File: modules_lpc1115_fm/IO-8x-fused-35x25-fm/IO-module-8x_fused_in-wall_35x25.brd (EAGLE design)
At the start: 35 x 25 mm, 87 parts, among them IC1 LPC1115, IC2 ATAES132A-SHEQ-T, Q2 ASFL, U1 EEPROM, X3 MICROMATCH-10

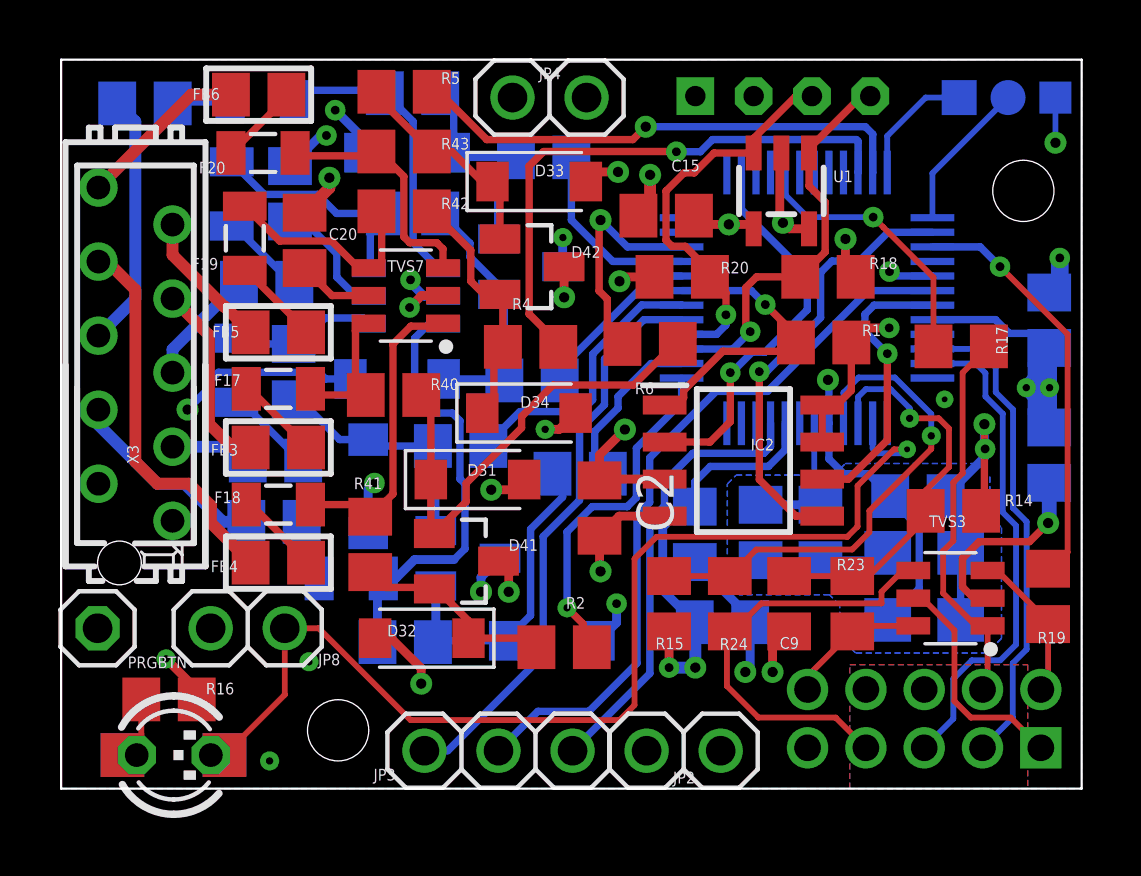
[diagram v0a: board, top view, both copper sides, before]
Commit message: [IOmodule8xUP] - some minor optimizations
corrected mixed up SWDIO / SWCLK labels
optimized some vias
optimized schematic
added ferrite values
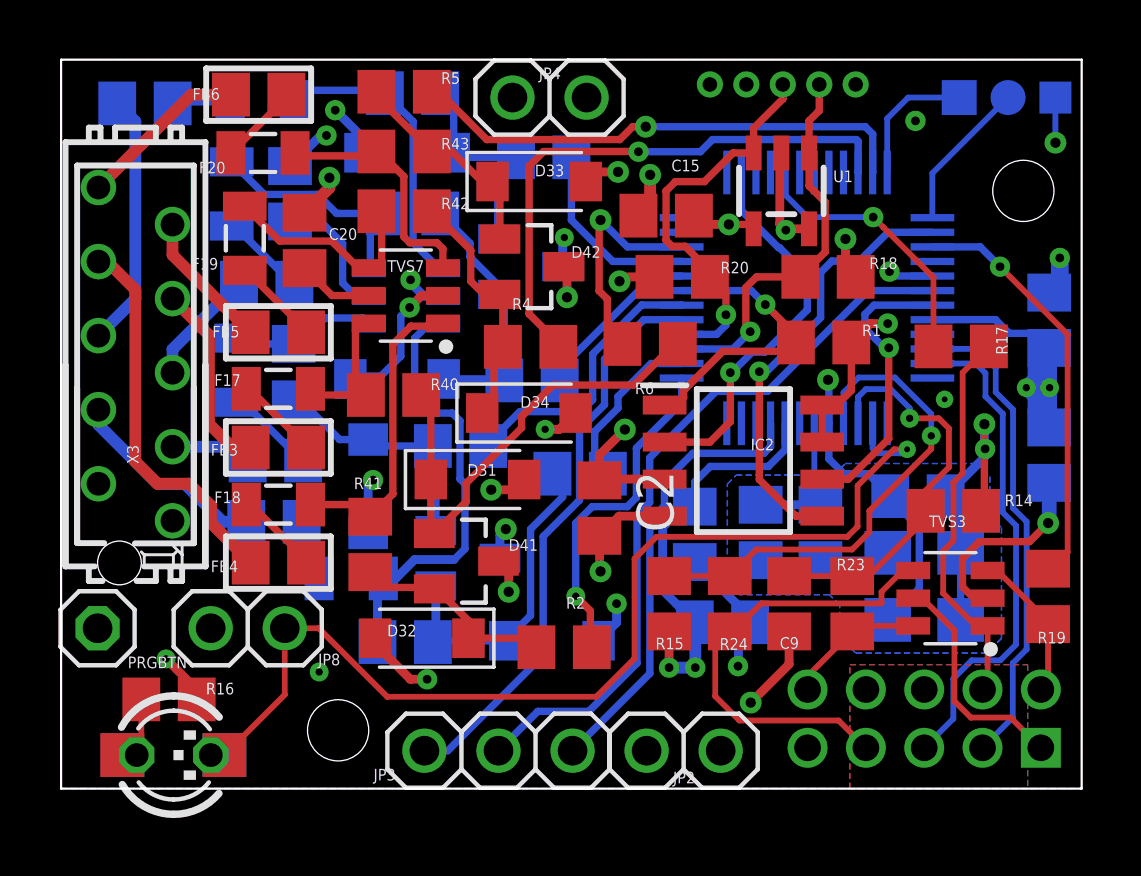
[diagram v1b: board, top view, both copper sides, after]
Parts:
- FB10, FB3, FB4, FB5, FB6, FB7, FB8, FB9: value (none) -> 1.5kΩ@100MHz
- JP1: value B4B-PH-K-S -> 653005114822; device con-JST PH:B4B-PH-K-S -> Wurth_Connectors_WR-WTB:653005114822
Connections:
- net SWD_SWCLK: now also JP7.4, R17.2, TVS3.1; no longer JP7.2, R19.2, TVS3.3
- net SWD_SWDIO: now also JP7.2, R19.2, TVS3.3; no longer JP7.4, R17.2, TVS3.1
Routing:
- net SWD_SWDIO: track 13.4 -> 5.23 mm
- net SWD_SWCLK: track 5.23 -> 13.4 mm
- net PROG: track 38.6 -> 37.0 mm
- net GND: track 60.5 -> 59.5 mm, vias 25 -> 24
- net SWD_ISP_EN: track 14.9 -> 15.7 mm
- net SCL: track 14.0 -> 13.5 mm

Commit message: [IOmodule8xUP] - breaking change of routing, I2C optimization
re-routed some IOs to other ARM pins
added 2nd alternative to connect I2C peripherals
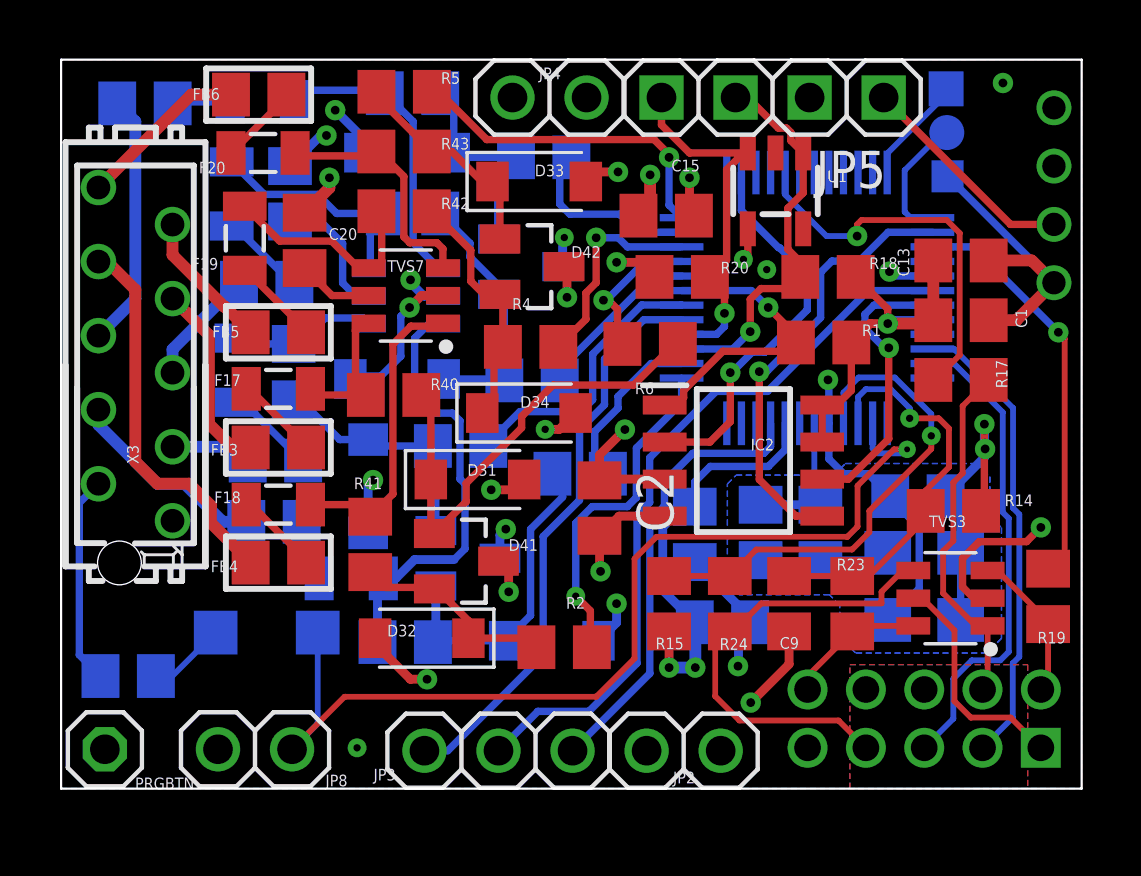
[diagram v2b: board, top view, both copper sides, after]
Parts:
- removed LED2: red, led:LED3MM
- removed LED3: red SMD, led:CHIPLED_1206
- added JP5: (no value), pinhead_dmx:1X04
- JP1: value 653005114822 -> 62000411622; device Wurth_Connectors_WR-WTB:653005114822 -> Eagle_WR-WTB (rev22a):62000411622
- moved JP1 9.34 mm to (33.5, 20.4), turned to 270 degrees
- moved C13 7.33 mm to (30.9, 18.1), flipped to the top, turned to 180 degrees
- moved LED1 5.28 mm to (7.05, 5.35), flipped to the bottom, turned to 90 degrees
- moved GND 4.58 mm to (30.4, 21.0)
- moved JP8 4.16 mm to (6.65, 1.35)
- moved PRGBTN 4.16 mm to (1.50, 1.35)
- moved C1 3.03 mm to (30.9, 16.1), flipped to the top, turned to 180 degrees
- moved RXD 2.42 mm to (30.4, 22.5)
- moved R16 1.61 mm to (2.30, 3.86), flipped to the bottom
- moved R17 1.15 mm to (30.9, 14.0)
- moved TXD 0.54 mm to (30.4, 24.0)
- moved U1 0.20 mm to (24.5, 20.5)
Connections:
- net +3V3: now also JP5.1
- net GND: now also JP5.2
- net IO4: now also IC1.23; no longer IC1.21
- net IO5: now also IC1.21; no longer IC1.22
- net IO7: now also IC1.22; no longer IC1.34
- net IO8: now also IC1.24; no longer IC1.35
- net N$41: no longer LED2.A, LED3.A
- net PROG: no longer LED2.K, LED3.C
- net SCL: now also JP5.3
- net SDA: now also JP5.4
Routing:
- net SDA: track 13.7 -> 27.1 mm
- net SCL: track 13.5 -> 25.9 mm
- net IO7: track 19.4 -> 7.34 mm
- net +3V3: track 65.0 -> 73.0 mm, vias 16 -> 13
- net IO8: track 17.4 -> 11.4 mm
- net SWCLK: track 9.39 -> 13.4 mm
- net IO5: track 7.76 -> 5.17 mm
- net GND: track 59.5 -> 61.8 mm, vias 24 -> 21
- net PROG: track 37.0 -> 34.7 mm
- net SWD_SWCLK: track 13.4 -> 12.2 mm
- net DBG_TXD: track 4.62 -> 3.71 mm
- net DBG_RXD: track 5.19 -> 4.44 mm
- net N$41: track 3.37 -> 2.67 mm
- net ISP_RXD: track 16.5 -> 15.9 mm
- net ISP_TXD: track 17.1 -> 16.5 mm
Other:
- board text added: "IO module fused 8x v1.0.0 beta2"
- board text added: "selfbus.org"

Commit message: [IOmodule8xUP] - changed values to standard values
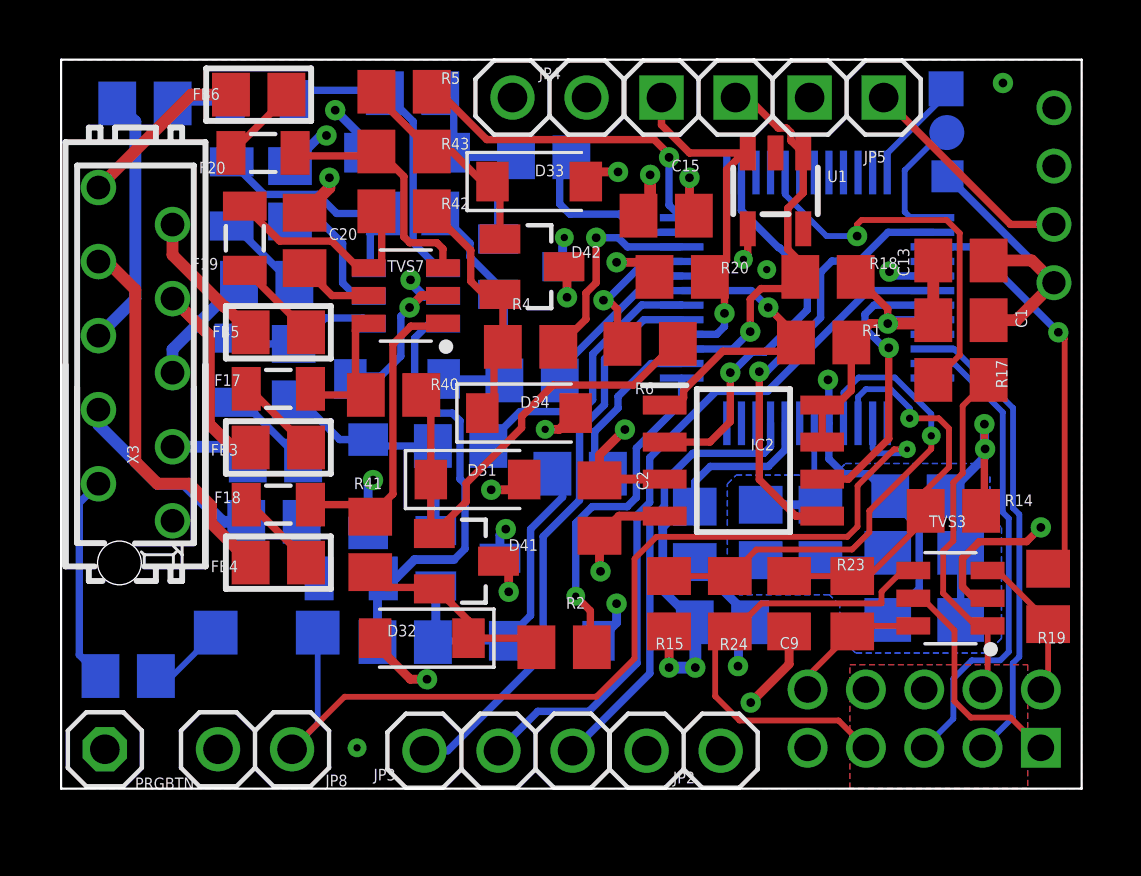
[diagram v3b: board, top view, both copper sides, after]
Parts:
- C1, C12, C15, C2, C20, C21: value 100n -> 100nF
- C11, C13: value 1µ -> 1uF
- C14, C9: value 10n -> 10nF
- C7: value 220p -> 220pF
- C8: value 100p -> 100pF
